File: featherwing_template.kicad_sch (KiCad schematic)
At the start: 0 parts

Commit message: Add headers
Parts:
- added J1: Conn_01x16_Socket, Connector_PinSocket_2.54mm:PinSocket_1x16_P2.54mm_Vertical, symbol Connector:Conn_01x16_Socket
- added J2: Conn_01x12_Socket, Connector_PinSocket_2.54mm:PinSocket_1x12_P2.54mm_Vertical, symbol Connector:Conn_01x12_Socket
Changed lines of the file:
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@@
 	(generator_version "9.0")
 	(paper "A4")
+	(symbol
+		(lib_id "Connector:Conn_01x12_Socket")
+		(at 124.46 53.34 0)
+		(unit 1)
+		(exclude_from_sim no)
+		(in_bom yes)
+		(on_board yes)
+		(dnp no)
+		(property "Reference" "J2"
+			(at 125.73 53.3399 0)
+			(effects
+				(font
+					(size 1.27 1.27)
+				)
+				(justify left)
+			)
+		)
+		(property "Value" "Conn_01x12_Socket"
+			(at 125.73 55.8799 0)
+			(effects
+				(font
+					(size 1.27 1.27)
+				)
+				(justify left)
+			)
+		)
+		(property "Footprint" "Connector_PinSocket_2.54mm:PinSocket_1x12_P2.54mm_Vertical"
+			(at 124.46 53.34 0)
+			(effects
+				(font
+					(size 1.27 1.27)
+				)
+				(hide yes)
+			)
+		)
+		(property "Datasheet" "~"
+			(at 124.46 53.34 0)
+			(effects
+				(font
+					(size 1.27 1.27)
+				)
+				(hide yes)
+			)
+		)
+		(property "Description" "Generic connector, single row, 01x12, script generated"
+			(at 124.46 53.34 0)
+			(effects
+				(font
+					(size 1.27 1.27)
+				)
+				(hide yes)
+			)
+		)
+		(pin "1"
+		)
+		(pin "2"
+		)
+		(pin "3"
+		)
+		(pin "4"
+		)
+		(pin "5"
+		)
+		(pin "6"
+		)
+		(pin "7"
+		)
+		(pin "8"
+		)
+		(pin "9"
+		)
+		(pin "10"
+		)
+		(pin "11"
+		)
+		(pin "12"
+		)
+		(instances
+			(project ""
+				(path "/b7a0c7d4-887a-4f70-85b6-b9a59be4c275"
+					(reference "J2")
+					(unit 1)
+				)
+			)
+		)
+	)
+	(symbol
+		(lib_id "Connector:Conn_01x16_Socket")
+		(at 96.52 52.07 0)
+		(unit 1)
+		(exclude_from_sim no)
+		(in_bom yes)
+		(on_board yes)
+		(dnp no)
+		(fields_autoplaced yes)
+		(property "Reference" "J1"
+			(at 97.79 52.0699 0)
+			(effects
+				(font
+					(size 1.27 1.27)
+				)
+				(justify left)
+			)
+		)
+		(property "Value" "Conn_01x16_Socket"
+			(at 97.79 54.6099 0)
+			(effects
+				(font
+					(size 1.27 1.27)
+				)
+				(justify left)
+			)
+		)
+		(property "Footprint" "Connector_PinSocket_2.54mm:PinSocket_1x16_P2.54mm_Vertical"
+			(at 96.52 52.07 0)
+			(effects
+				(font
+					(size 1.27 1.27)
+				)
+				(hide yes)
+			)
+		)
+		(property "Datasheet" "~"
+			(at 96.52 52.07 0)
+			(effects
+				(font
+					(size 1.27 1.27)
+				)
+				(hide yes)
+			)
+		)
+		(property "Description" "Generic connector, single row, 01x16, script generated"
+			(at 96.52 52.07 0)
+			(effects
+				(font
+					(size 1.27 1.27)
+				)
+				(hide yes)
+			)
+		)
+		(pin "1"
+		)
+		(pin "2"
+		)
+		(pin "10"
+		)
+		(pin "11"
+		)
+		(pin "15"
+		)
+		(pin "16"
+		)
+		(pin "12"
+		)
+		(pin "13"
+		)
+		(pin "14"
+		)
+		(pin "3"
+		)
+		(pin "4"
+		)
+		(pin "5"
+		)
+		(pin "6"
+		)
+		(pin "7"
+		)
+		(pin "8"
+		)
+		(pin "9"
+		)
+		(instances
+			(project ""
+				(path "/b7a0c7d4-887a-4f70-85b6-b9a59be4c275"
+					(reference "J1")
+					(unit 1)
+				)
+			)
+		)
+	)
 	(sheet_instances
 		(path "/"

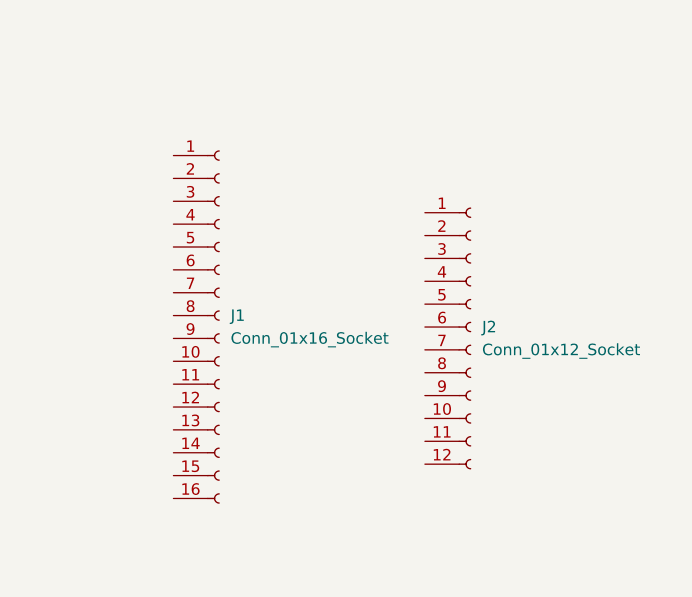
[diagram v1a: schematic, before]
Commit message: Add plated mounting holes
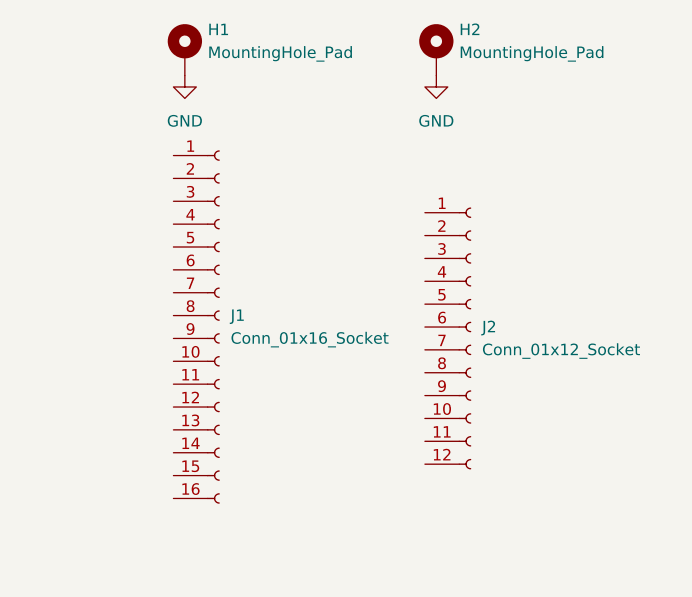
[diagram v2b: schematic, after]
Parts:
- added H1, H2: MountingHole_Pad, custom:MountingHole_2.5mm, symbol Mechanical:MountingHole_Pad
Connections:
- new net GND: H1.1, H2.1

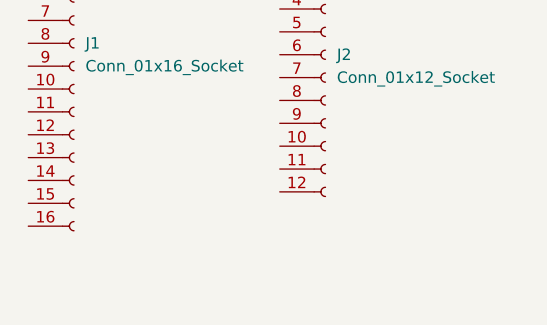
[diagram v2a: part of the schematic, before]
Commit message: Add nonplated mounting holes
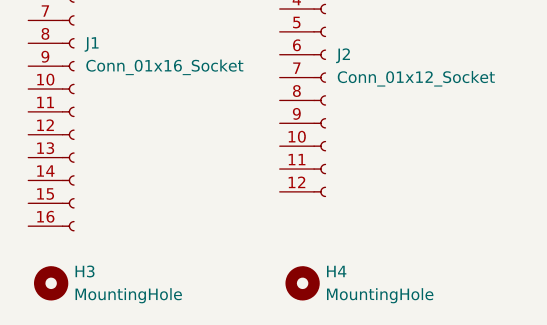
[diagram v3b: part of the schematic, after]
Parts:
- added H3, H4: MountingHole, MountingHole:MountingHole_2.5mm, symbol Mechanical:MountingHole
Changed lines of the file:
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@@
 	(paper "A4")
+	(symbol
+		(lib_id "Mechanical:MountingHole")
+		(at 121.92 78.74 0)
+		(unit 1)
+		(exclude_from_sim no)
+		(in_bom no)
+		(on_board yes)
+		(dnp no)
+		(fields_autoplaced yes)
+		(property "Reference" "H4"
+			(at 124.46 77.4699 0)
+			(effects
+				(font
+					(size 1.27 1.27)
+				)
+				(justify left)
+			)
+		)
+		(property "Value" "MountingHole"
+			(at 124.46 80.0099 0)
+			(effects
+				(font
+					(size 1.27 1.27)
+				)
+				(justify left)
+			)
+		)
+		(property "Footprint" "MountingHole:MountingHole_2.5mm"
+			(at 121.92 78.74 0)
+			(effects
+				(font
+					(size 1.27 1.27)
+				)
+				(hide yes)
+			)
+		)
+		(property "Datasheet" "~"
+			(at 121.92 78.74 0)
+			(effects
+				(font
+					(size 1.27 1.27)
+				)
+				(hide yes)
+			)
+		)
+		(property "Description" "Mounting Hole without connection"
+			(at 121.92 78.74 0)
+			(effects
+				(font
+					(size 1.27 1.27)
+				)
+				(hide yes)
+			)
+		)
+		(instances
+			(project ""
+				(path "/b7a0c7d4-887a-4f70-85b6-b9a59be4c275"
+					(reference "H4")
+					(unit 1)
+				)
+			)
+		)
+	)
 	(symbol
 		(lib_id "Mechanical:MountingHole_Pad")
@@
 					(unit 1)
 				)
+			)
+		)
+	)
+	(symbol
+		(lib_id "Mechanical:MountingHole")
+		(at 93.98 78.74 0)
+		(unit 1)
+		(exclude_from_sim no)
+		(in_bom no)
+		(on_board yes)
+		(dnp no)
+		(fields_autoplaced yes)
+		(property "Reference" "H3"
+			(at 96.52 77.4699 0)
+			(effects
+				(font
+					(size 1.27 1.27)
+				)
+				(justify left)
+			)
+		)
+		(property "Value" "MountingHole"
+			(at 96.52 80.0099 0)
+			(effects
+				(font
+					(size 1.27 1.27)
+				)
+				(justify left)
+			)
+		)
+		(property "Footprint" "MountingHole:MountingHole_2.5mm"
+			(at 93.98 78.74 0)
+			(effects
+				(font
+					(size 1.27 1.27)
+				)
+				(hide yes)
+			)
+		)
+		(property "Datasheet" "~"
+			(at 93.98 78.74 0)
+			(effects
+				(font
+					(size 1.27 1.27)
+				)
+				(hide yes)
+			)
+		)
+		(property "Description" "Mounting Hole without connection"
+			(at 93.98 78.74 0)
+			(effects
+				(font
+					(size 1.27 1.27)
+				)
+				(hide yes)
+			)
+		)
+		(instances
+			(project ""
+				(path "/b7a0c7d4-887a-4f70-85b6-b9a59be4c275"
+					(reference "H3")
+					(unit 1)
+				)

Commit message: Add known nets to the sockets
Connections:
- net GND: now also J1.4 (Pin_4)
- net +BATT: now reaches J2.1 (Pin_1)
- net SCL: now reaches J2.11 (Pin_11)
- net SDA: now reaches J2.12 (Pin_12)
- net EN: now reaches J2.2 (Pin_2)
- net USB: now reaches J2.3 (Pin_3)
- net RST: now reaches J1.1 (Pin_1)
- net SCK: now reaches J1.11 (Pin_11)
- net MO: now reaches J1.12 (Pin_12)
- net MI: now reaches J1.13 (Pin_13)
- net RX: now reaches J1.14 (Pin_14)
- net TX: now reaches J1.15 (Pin_15)
- net +3.3V: now reaches J1.2 (Pin_2)
